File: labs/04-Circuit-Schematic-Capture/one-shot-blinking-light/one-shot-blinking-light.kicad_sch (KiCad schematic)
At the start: 22 parts, among them J101 Push Button, J102 LED, J103 Power Switch, SW101 Power Switch, SW102 SW_Push, U101 LM7805_TO220, U102 74LVC1G08

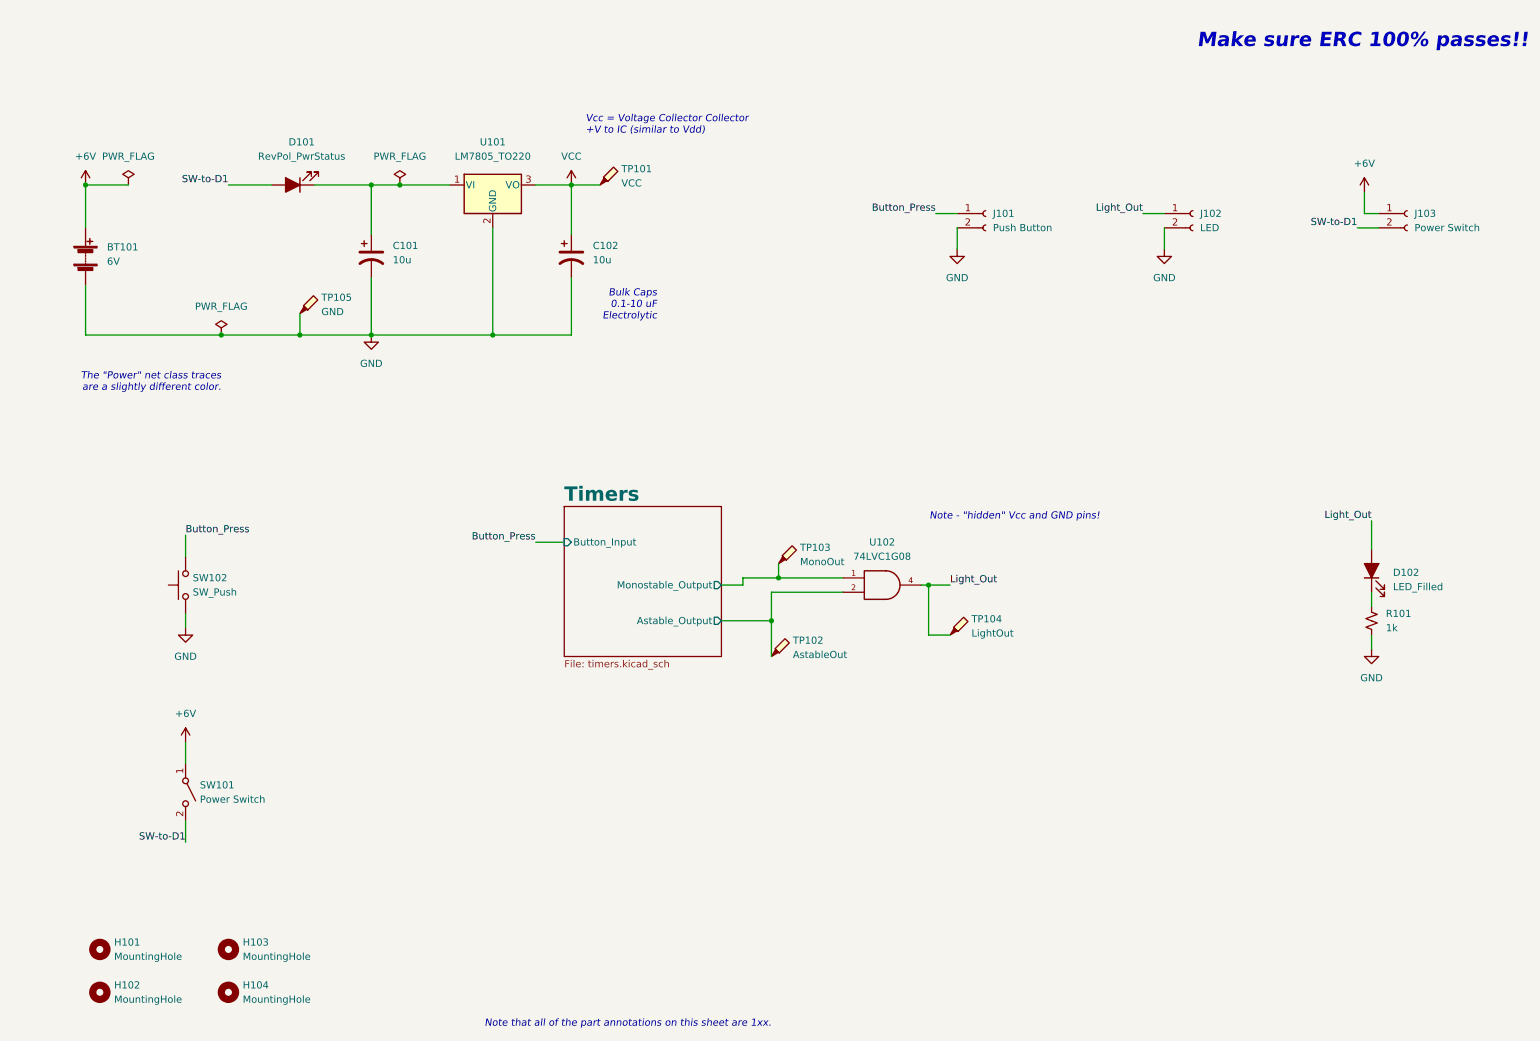
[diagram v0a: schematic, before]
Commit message: exclude mounting holes from BOM; add more annotation
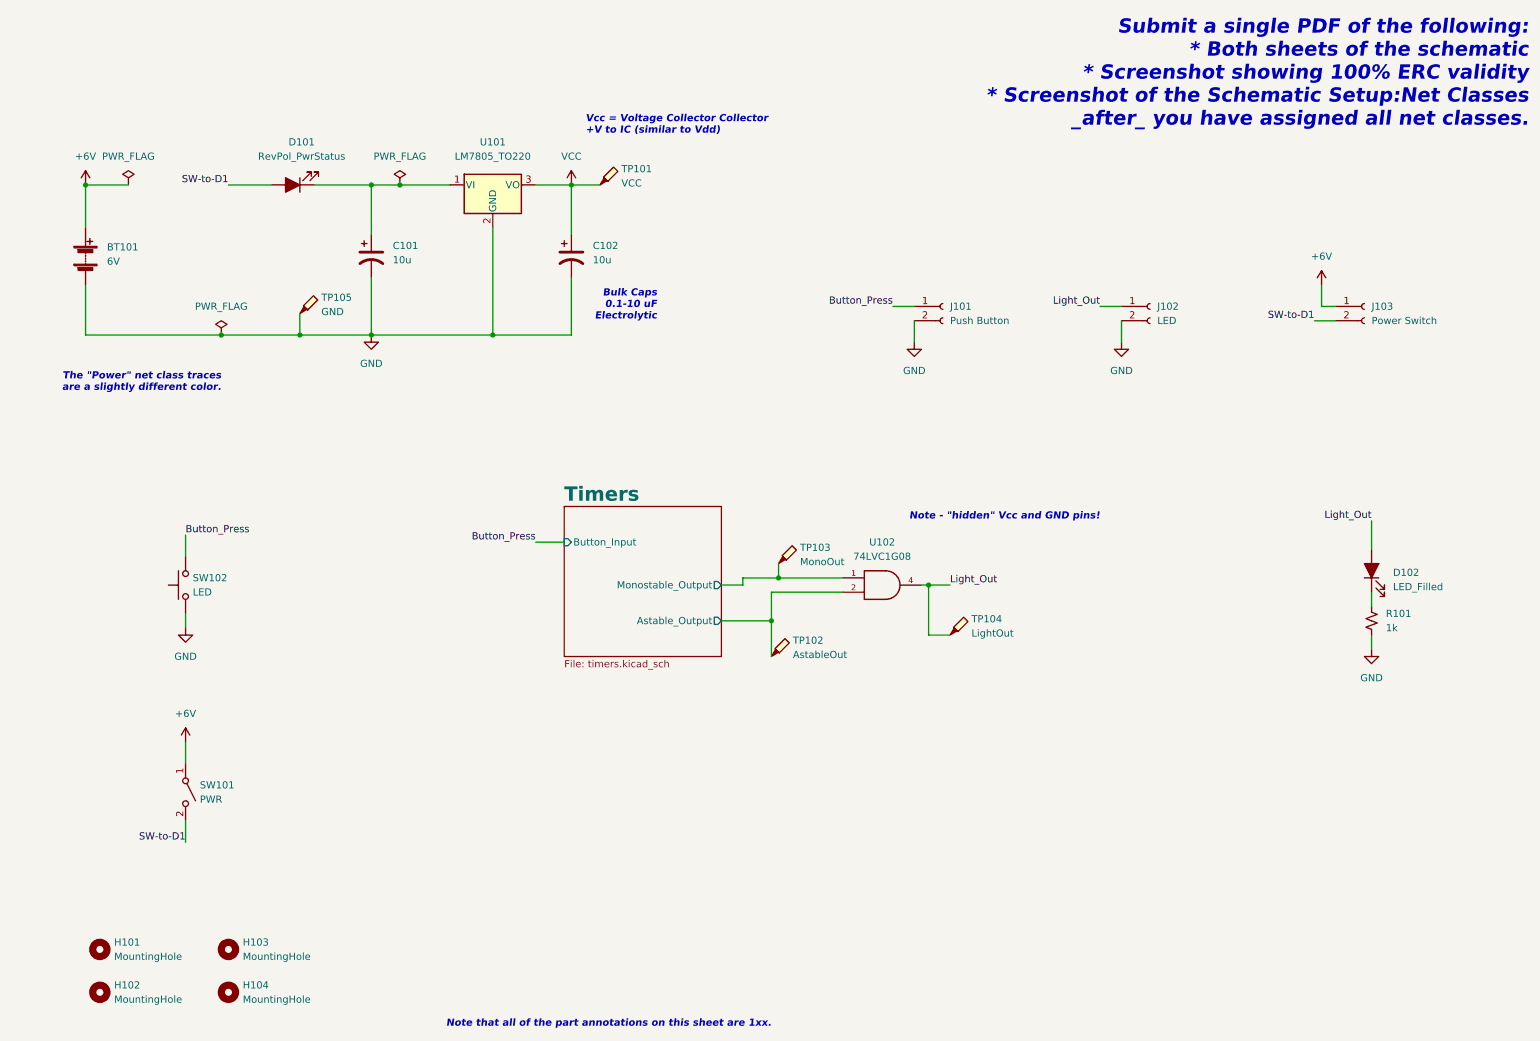
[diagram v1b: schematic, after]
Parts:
- H101, H102, H103, H104: now left out of the parts list
- SW101: value Power Switch -> PWR
- SW102: value SW_Push -> LED
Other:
- note added: "Submit a single PDF of the following: * Both sheets of the schematic * Screenshot showing 100% ERC validity * Screenshot of the Schematic Setup:Net Classes _after_ you have assigned all net classes."
- note removed: "Make sure ERC 100% passes!!"
- moved on the sheet: J101, J102, J103
